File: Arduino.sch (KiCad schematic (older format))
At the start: 25 parts, among them J1 ISP, SW1 Reset, U1 ATMEGA32U4-AU, Y1 16MHz

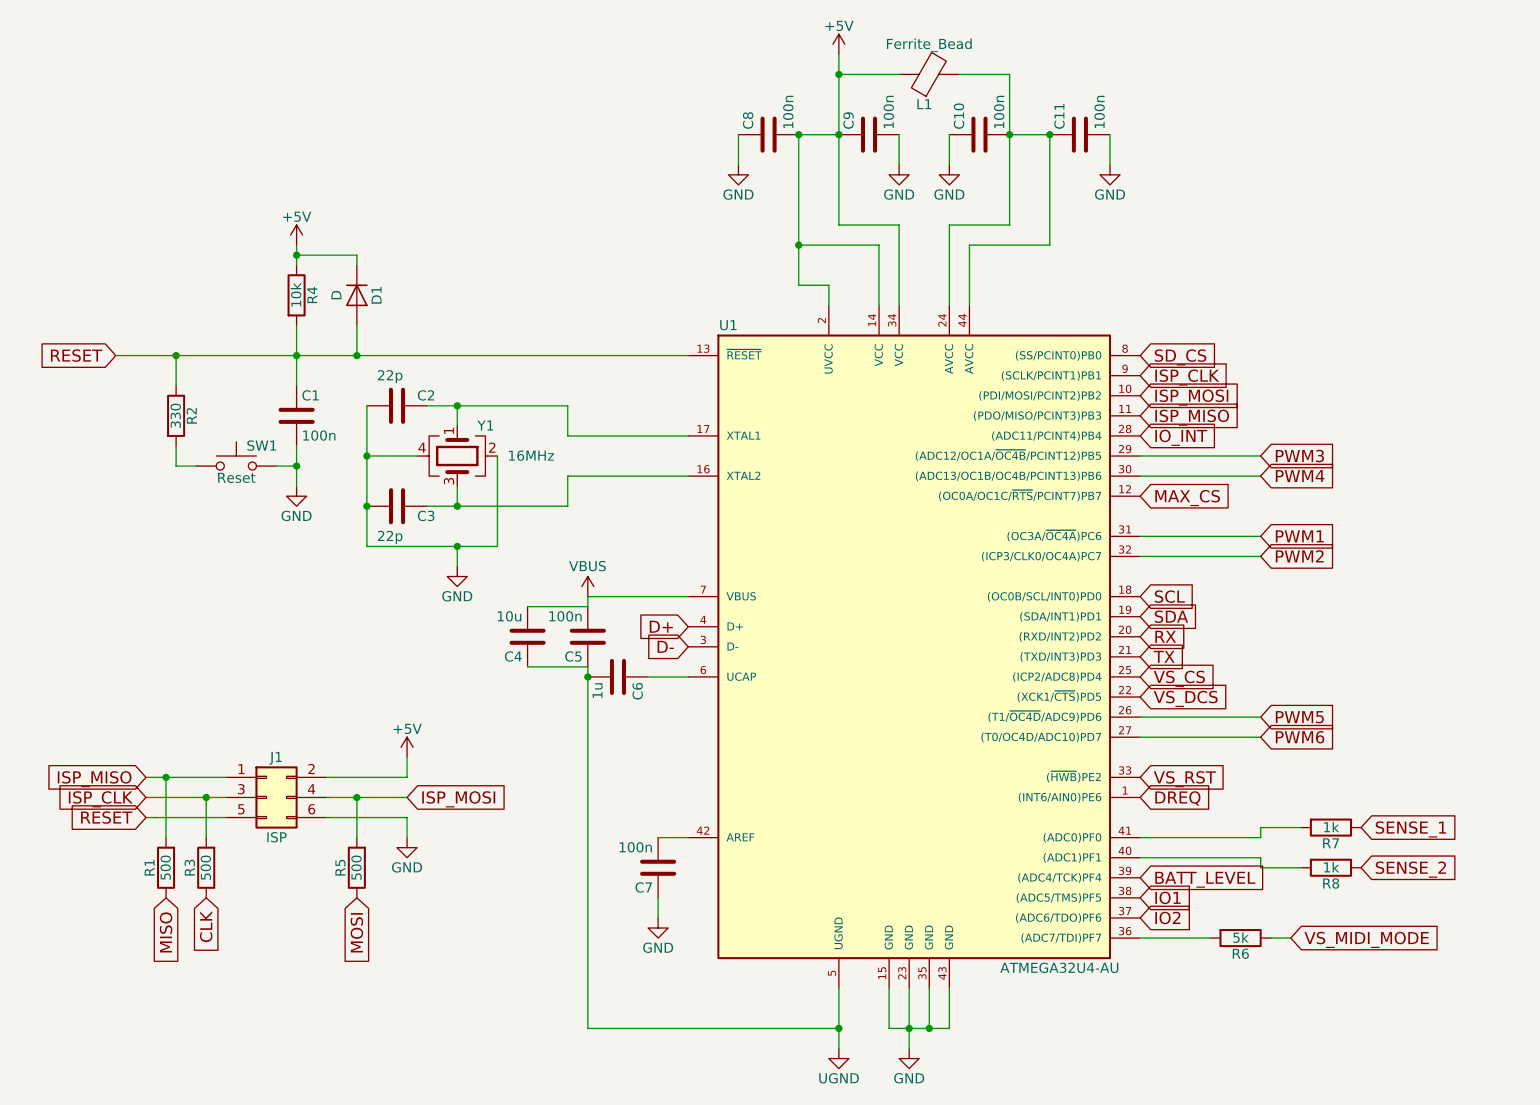
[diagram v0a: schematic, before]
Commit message: Board should be ok. Bargraph leds yet to do.
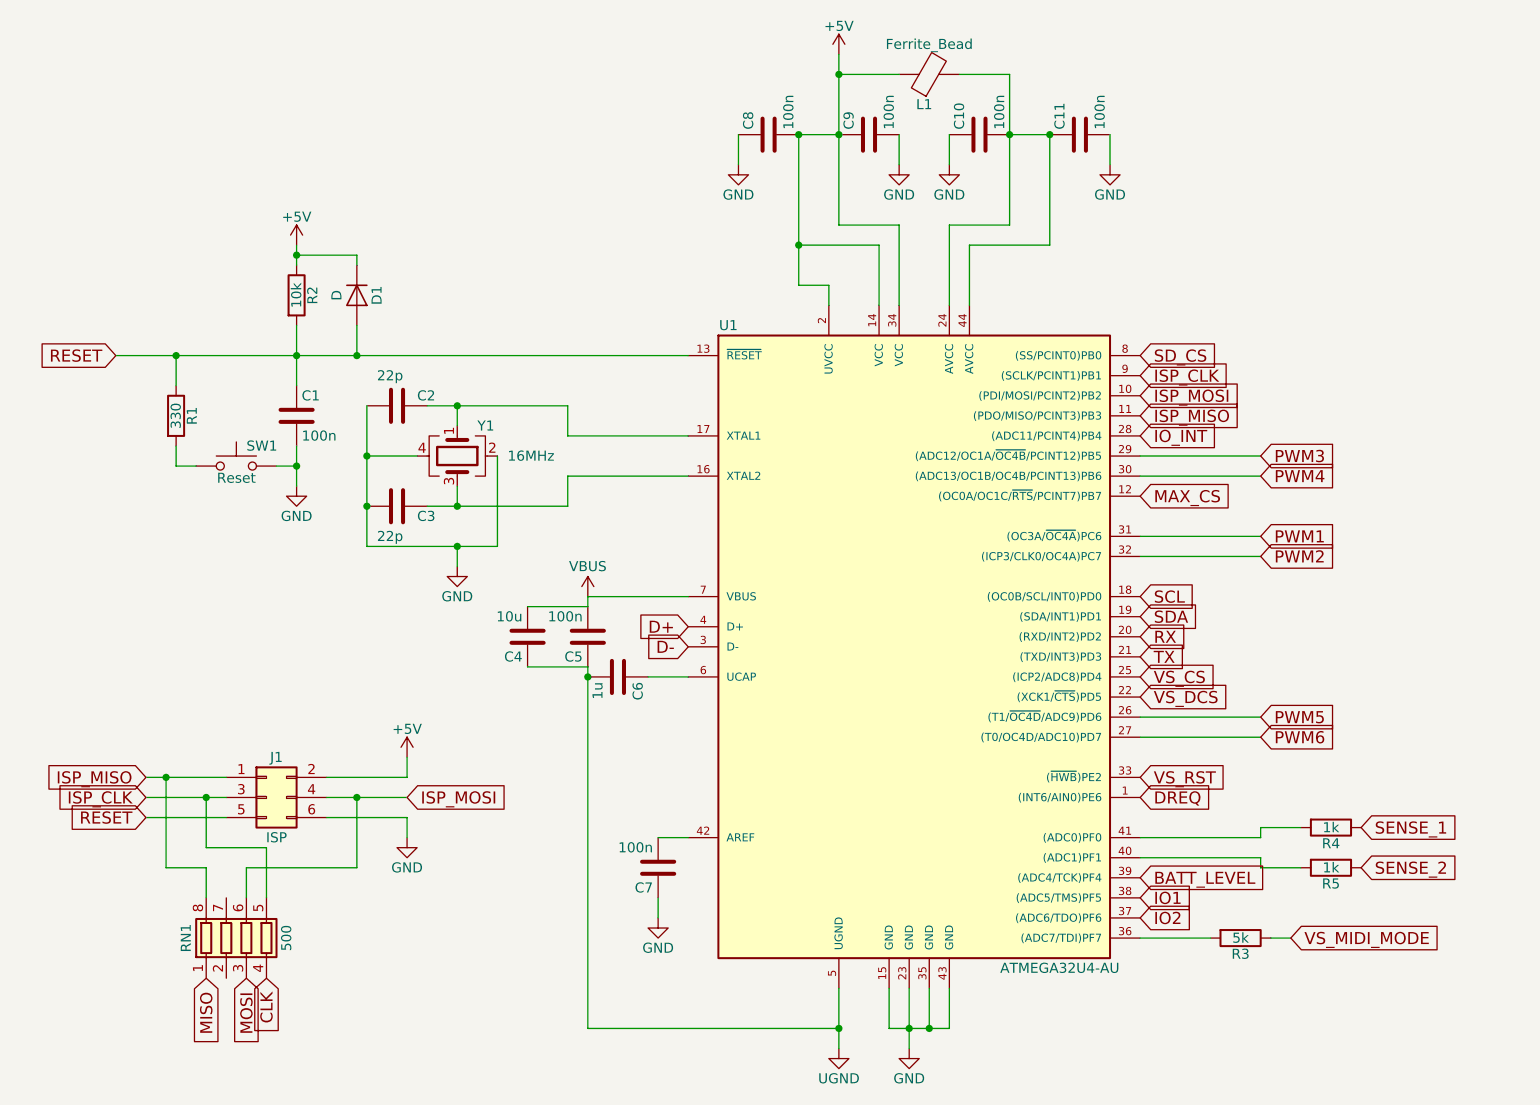
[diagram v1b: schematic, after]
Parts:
- removed R1, R3, R5: 500, Resistors_SMD:R_0603, symbol R
- added RN1: 500, Resistors_SMD:R_Array_Concave_4x0603, symbol R_Pack04
- renumbered R2 to R1, R4 to R2, R6 to R3, R7 to R4, R8 to R5
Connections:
- net CLK: now also RN1.4 (R4.1)
- net ISP_CLK: now also RN1.5 (R4.2)
- net ISP_MISO: now also RN1.8 (R1.2)
- net ISP_MOSI: now also RN1.6 (R3.2)
- net MISO: now also RN1.1 (R1.1)
- net MOSI: now also RN1.3 (R3.1)
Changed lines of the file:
@@
 RESET
 $Comp
-L R R4
+L R R2
 U 1 1 59A745F3
 P 1950 2050
-F 0 "R4" V 2030 2050 50  0000 C CNN
+F 0 "R2" V 2030 2050 50  0000 C CNN
 F 1 "10k" V 1950 2050 50  0000 C CNN
 F 2 "Resistors_SMD:R_0603" V 1880 2050 50  0001 C CNN
@@
 $EndComp
 $Comp
-L R R2
+L R R1
 U 1 1 59A75000
 P 1350 2650
-F 0 "R2" V 1430 2650 50  0000 C CNN
+F 0 "R1" V 1430 2650 50  0000 C CNN
 F 1 "330" V 1350 2650 50  0000 C CNN
 F 2 "Resistors_SMD:R_0603" V 1280 2650 50  0001 C CNN
@@
 	1    2500 4350
 	1    0    0    -1
-$EndComp
-$Comp
-L R R5
-U 1 1 59A7C3EE
-P 2250 4900
-F 0 "R5" V 2330 4900 50  0000 C CNN
-F 1 "500" V 2250 4900 50  0000 C CNN
-F 2 "Resistors_SMD:R_0603" V 2180 4900 50  0001 C CNN
-F 3 "" H 2250 4900 50  0001 C CNN
-	1    2250 4900
-	-1   0    0    1
 $EndComp
 Text GLabel 6150 2450 2    60   Input ~ 0
@@
 	1    0    0    -1
 $EndComp
-$Comp
-L R R1
-U 1 1 59A7CE6D
-P 1300 4900
-F 0 "R1" V 1380 4900 50  0000 C CNN
-F 1 "500" V 1300 4900 50  0000 C CNN
-F 2 "Resistors_SMD:R_0603" V 1230 4900 50  0001 C CNN
-F 3 "" H 1300 4900 50  0001 C CNN
-	1    1300 4900
-	-1   0    0    1
-$EndComp
-$Comp
-L R R3
-U 1 1 59A7CEDD
-P 1500 4900
-F 0 "R3" V 1580 4900 50  0000 C CNN
-F 1 "500" V 1500 4900 50  0000 C CNN
-F 2 "Resistors_SMD:R_0603" V 1430 4900 50  0001 C CNN
-F 3 "" H 1500 4900 50  0001 C CNN
-	1    1500 4900
-	-1   0    0    1
-$EndComp
-Text GLabel 1300 5050 3    60   Input ~ 0
+Text GLabel 1500 5450 3    60   Input ~ 0
 MISO
-Text GLabel 2250 5050 3    60   Input ~ 0
+Text GLabel 1700 5450 3    60   Input ~ 0
 MOSI
-Text GLabel 1500 5050 3    60   Input ~ 0
+Text GLabel 1800 5450 3    60   Input ~ 0
 CLK
 $Comp
@@
 	2500 4450 2500 4350
 Wire Wire Line
-	1300 4750 1300 4450
+	1300 4450 1300 4900
 Connection ~ 1300 4450
 Wire Wire Line
-	1500 4750 1500 4550
+	1500 4550 1500 4800
 Connection ~ 1500 4550
 Wire Wire Line
-	2250 4550 2250 4750
+	2250 4550 2250 4900
 Connection ~ 2250 4550
 Wire Wire Line
@@
 VS_MIDI_MODE
 $Comp
-L R R6
+L R R3
 U 1 1 59B1BBE0
 P 6650 5250
-F 0 "R6" V 6730 5250 50  0000 C CNN
+F 0 "R3" V 6730 5250 50  0000 C CNN
 F 1 "5k" V 6650 5250 50  0000 C CNN
 F 2 "Resistors_SMD:R_0603" V 6580 5250 50  0001 C CNN
@@
 	6800 5250 6900 5250
 $Comp
-L R R7
+L R R4
 U 1 1 59C9C3BA
 P 7100 4700
-F 0 "R7" V 7180 4700 50  0000 C CNN
+F 0 "R4" V 7180 4700 50  0000 C CNN
 F 1 "1k" V 7100 4700 50  0000 C CNN
 F 2 "Resistors_SMD:R_0603" V 7030 4700 50  0001 C CNN
@@
 $EndComp
 $Comp
-L R R8
+L R R5
 U 1 1 59C9C547
 P 7100 4900
-F 0 "R8" V 7180 4900 50  0000 C CNN
+F 0 "R5" V 7180 4900 50  0000 C CNN
 F 1 "1k" V 7100 4900 50  0000 C CNN
 F 2 "Resistors_SMD:R_0603" V 7030 4900 50  0001 C CNN
@@
 Wire Wire Line
 	6750 4850 6150 4850
+$Comp
+L R_Pack04 RN1
+U 1 1 59CC0F73
+P 1700 5250
+F 0 "RN1" V 1400 5250 50  0000 C CNN
+F 1 "500" V 1900 5250 50  0000 C CNN
+F 2 "Resistors_SMD:R_Array_Concave_4x0603" V 1975 5250 50  0001 C CNN
+F 3 "" H 1700 5250 50  0001 C CNN
+	1    1700 5250
+	1    0    0    -1
+$EndComp
+Wire Wire Line
+	1300 4900 1500 4900
+Wire Wire Line
+	1500 4900 1500 5050
+Wire Wire Line
+	2250 4900 1700 4900
+Wire Wire Line
+	1700 4900 1700 5050
+Wire Wire Line
+	1500 4800 1800 4800
+Wire Wire Line
+	1800 4800 1800 5050
 $EndSCHEMATC

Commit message: Board modified after ckecking. Ready for fab, just need to create gerber, position and components files.
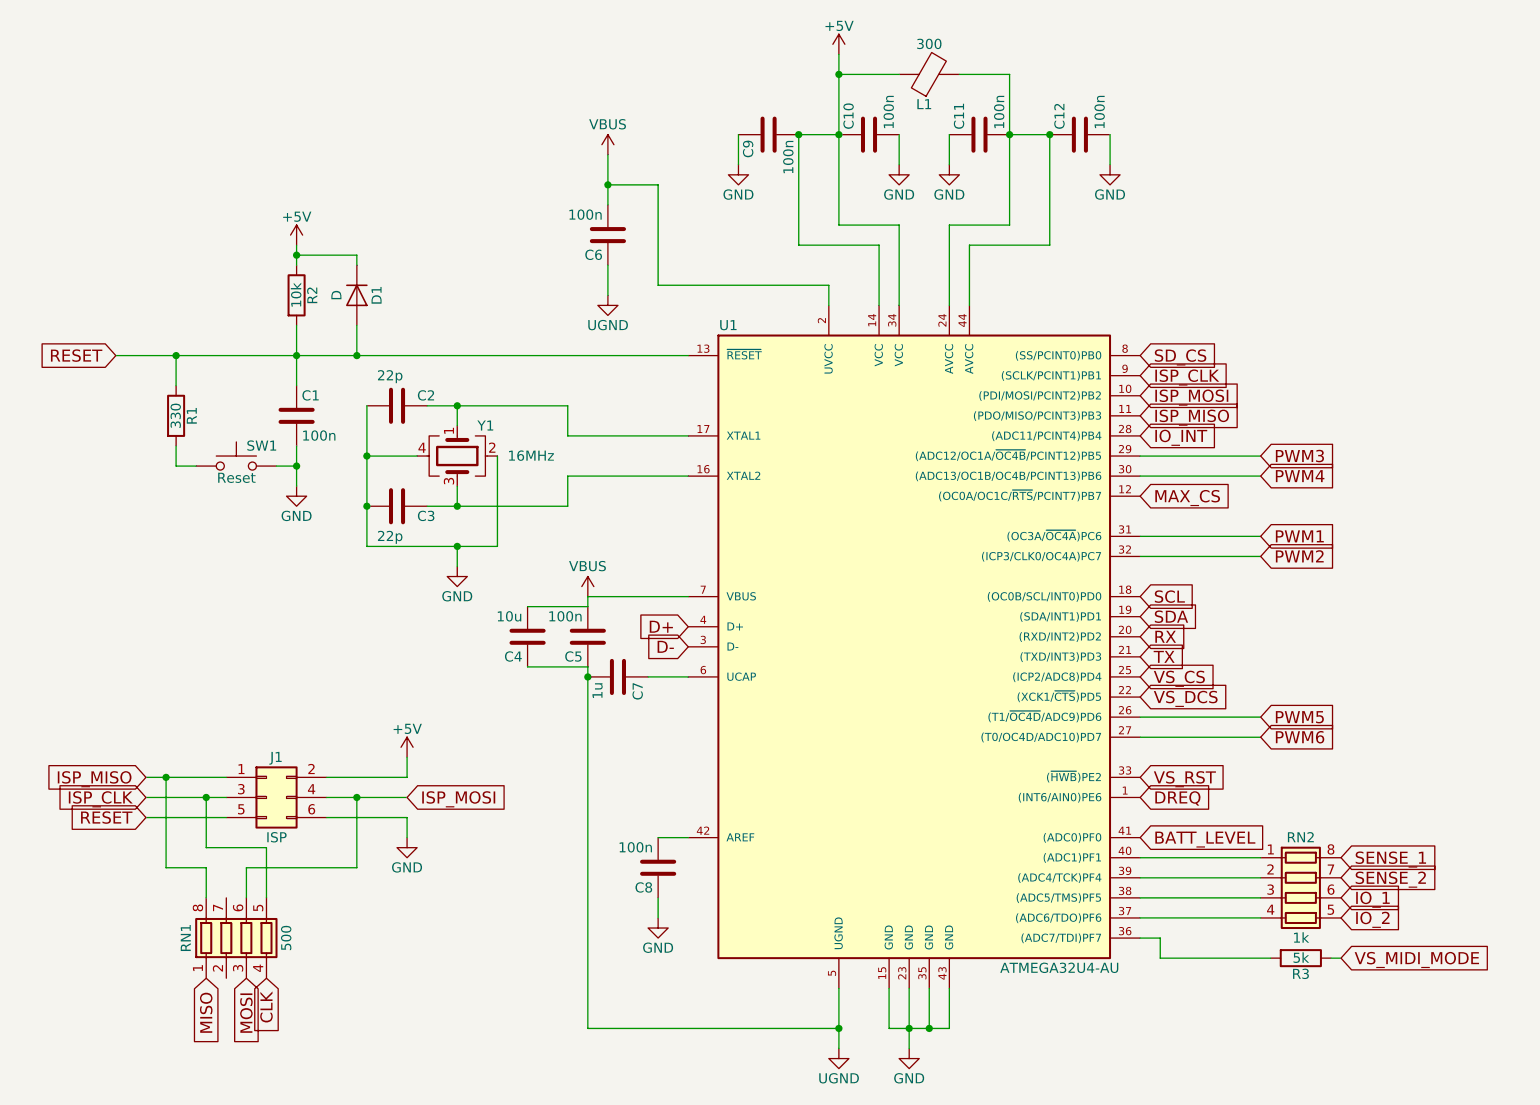
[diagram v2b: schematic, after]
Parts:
- removed R4, R5: 1k, Resistors_SMD:R_0603, symbol R
- added C6: 100n, Capacitors_SMD:C_0603, symbol C
- added RN2: 1k, Resistors_SMD:R_Array_Concave_4x0603, symbol R_Pack04
- L1: value Ferrite_Bead -> 300
- renumbered C9 to C10, C10 to C11, C11 to C12, C6 to C7, C7 to C8, C8 to C9
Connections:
- net +5V: no longer U1.2 (UVCC)
- net BATT_LEVEL: now also U1.41 ((ADC0)PF0); no longer U1.39 ((ADC4/TCK)PF4)
- net SENSE_1: now also RN2.8 (R1.2)
- net SENSE_2: now also RN2.7 (R2.2)
- net UGND: now also C6.1
- net VBUS: now also U1.2 (UVCC), C6.2
- net at U1.40 ((ADC1)PF1): now also RN2.1 (R1.1)
- net IO1: no longer names the net of U1.38 ((ADC5/TMS)PF5)
- net IO1: now also RN2.3 (R3.1)
- net IO2: no longer names the net of U1.37 ((ADC6/TDO)PF6)
- net IO2: now also RN2.4 (R4.1)
- new net: RN2.2 (R2.1), U1.39 ((ADC4/TCK)PF4)
- new net IO_1: RN2.6 (R3.2)
- new net IO_2: RN2.5 (R4.2)
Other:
- moved on the sheet: R3
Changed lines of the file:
@@
 EESchema Schematic File Version 2
+LIBS:ContactConsequencesMono-rescue
 LIBS:switches-perso
 LIBS:Logos
@@
 $EndComp
 $Comp
-L C C9
+L C C10
 U 1 1 59A733E9
 P 4800 1250
-F 0 "C9" H 4825 1350 50  0000 L CNN
+F 0 "C10" H 4825 1350 50  0000 L CNN
 F 1 "100n" H 4825 1150 50  0000 L CNN
 F 2 "Capacitors_SMD:C_0603" H 4838 1100 50  0001 C CNN
@@
 $EndComp
 $Comp
-L C C8
+L C C9
 U 1 1 59A734B6
 P 4300 1250
-F 0 "C8" H 4325 1350 50  0000 L CNN
+F 0 "C9" H 4325 1350 50  0000 L CNN
 F 1 "100n" H 4325 1150 50  0000 L CNN
 F 2 "Capacitors_SMD:C_0603" H 4338 1100 50  0001 C CNN
 F 3 "" H 4300 1250 50  0001 C CNN
 	1    4300 1250
-	0    -1   -1   0
+	0    -1   1    0
 $EndComp
 $Comp
@@
 $EndComp
 $Comp
-L C C10
+L C C11
 U 1 1 59A74301
 P 5350 1250
-F 0 "C10" H 5375 1350 50  0000 L CNN
+F 0 "C11" H 5375 1350 50  0000 L CNN
 F 1 "100n" H 5375 1150 50  0000 L CNN
 F 2 "Capacitors_SMD:C_0603" H 5388 1100 50  0001 C CNN
@@
 $EndComp
 $Comp
-L C C11
+L C C12
 U 1 1 59A7433B
 P 5850 1250
-F 0 "C11" H 5875 1350 50  0000 L CNN
+F 0 "C12" H 5875 1350 50  0000 L CNN
 F 1 "100n" H 5875 1150 50  0000 L CNN
 F 2 "Capacitors_SMD:C_0603" H 5888 1100 50  0001 C CNN
@@
 $EndComp
 $Comp
-L C C6
+L C C7
 U 1 1 59A9524E
 P 3550 3950
-F 0 "C6" H 3575 4050 50  0000 L CNN
+F 0 "C7" H 3575 4050 50  0000 L CNN
 F 1 "1u" H 3575 3850 50  0000 L CNN
 F 2 "Capacitors_SMD:C_0603" H 3588 3800 50  0001 C CNN
@@
 D+
 $Comp
-L C C7
+L C C8
 U 1 1 59A9601B
 P 3750 4900
-F 0 "C7" H 3775 5000 50  0000 L CNN
+F 0 "C8" H 3775 5000 50  0000 L CNN
 F 1 "100n" H 3775 4800 50  0000 L CNN
 F 2 "Capacitors_SMD:C_0603" H 3788 4750 50  0001 C CNN
@@
 Text GLabel 6150 3850 2    60   Input ~ 0
 TX
-Text GLabel 7250 4700 2    60   Input ~ 0
+Text GLabel 7150 4850 2    60   Input ~ 0
 SENSE_1
-Text GLabel 7250 4900 2    60   Input ~ 0
+Text GLabel 7150 4950 2    60   Input ~ 0
 SENSE_2
 Text GLabel 6150 2350 2    60   Input ~ 0
@@
 P 5100 950
 F 0 "L1" V 4950 975 50  0000 C CNN
-F 1 "Ferrite_Bead" V 5250 950 50  0000 C CNN
+F 1 "300" V 5250 950 50  0000 C CNN
 F 2 "Inductors_SMD:L_0603" V 5030 950 50  0001 C CNN
 F 3 "" H 5100 950 50  0001 C CNN
@@
 	0    -1   -1   0
 $EndComp
-Text GLabel 6150 4950 2    60   Input ~ 0
+Text GLabel 6150 4750 2    60   Input ~ 0
 BATT_LEVEL
 Text GLabel 6150 4450 2    60   Input ~ 0
@@
 Wire Wire Line
 	6150 4250 6750 4250
-Text GLabel 6150 5050 2    60   Input ~ 0
-IO1
-Text GLabel 6150 5150 2    60   Input ~ 0
-IO2
+Text GLabel 7150 5050 2    60   Input ~ 0
+IO_1
+Text GLabel 7150 5150 2    60   Input ~ 0
+IO_2
 Wire Wire Line
 	4450 1250 4650 1250
 Wire Wire Line
 	4850 1800 4450 1800
-Wire Wire Line
-	4450 1250 4450 2000
 Connection ~ 4450 1250
 Wire Wire Line
 	4600 2100 4600 2000
-Wire Wire Line
-	4600 2000 4450 2000
-Connection ~ 4450 1800
 Wire Wire Line
 	5300 1800 5300 2100
 Text GLabel 6150 2750 2    60   Input ~ 0
 IO_INT
-Text GLabel 6900 5250 2    60   Input ~ 0
+Text GLabel 7150 5350 2    60   Input ~ 0
 VS_MIDI_MODE
 $Comp
 L R R3
 U 1 1 59B1BBE0
-P 6650 5250
-F 0 "R3" V 6730 5250 50  0000 C CNN
-F 1 "5k" V 6650 5250 50  0000 C CNN
-F 2 "Resistors_SMD:R_0603" V 6580 5250 50  0001 C CNN
-F 3 "" H 6650 5250 50  0001 C CNN
-	1    6650 5250
+P 6950 5350
+F 0 "R3" V 7030 5350 50  0000 C CNN
+F 1 "5k" V 6950 5350 50  0000 C CNN
+F 2 "Resistors_SMD:R_0603" V 6880 5350 50  0001 C CNN
+F 3 "" H 6950 5350 50  0001 C CNN
+	1    6950 5350
 	0    1    1    0
 $EndComp
-Wire Wire Line
-	6150 5250 6500 5250
-Wire Wire Line
-	6800 5250 6900 5250
-$Comp
-L R R4
-U 1 1 59C9C3BA
-P 7100 4700
-F 0 "R4" V 7180 4700 50  0000 C CNN
-F 1 "1k" V 7100 4700 50  0000 C CNN
-F 2 "Resistors_SMD:R_0603" V 7030 4700 50  0001 C CNN
-F 3 "" H 7100 4700 50  0001 C CNN
-	1    7100 4700
-	0    1    1    0
-$EndComp
-$Comp
-L R R5
-U 1 1 59C9C547
-P 7100 4900
-F 0 "R5" V 7180 4900 50  0000 C CNN
-F 1 "1k" V 7100 4900 50  0000 C CNN
-F 2 "Resistors_SMD:R_0603" V 7030 4900 50  0001 C CNN
-F 3 "" H 7100 4900 50  0001 C CNN
-	1    7100 4900
-	0    1    1    0
-$EndComp
-Wire Wire Line
-	6150 4750 6750 4750
-Wire Wire Line
-	6750 4750 6750 4700
-Wire Wire Line
-	6750 4700 6950 4700
-Wire Wire Line
-	6950 4900 6750 4900
-Wire Wire Line
-	6750 4900 6750 4850
-Wire Wire Line
-	6750 4850 6150 4850
 $Comp
 L R_Pack04 RN1
@@
 Wire Wire Line
 	1800 4800 1800 5050
+Wire Wire Line
+	4450 1800 4450 1250
+$Comp
+L VBUS #PWR015
+U 1 1 59F06B7F
+P 3500 1350
+F 0 "#PWR015" H 3500 1200 50  0001 C CNN
+F 1 "VBUS" H 3500 1500 50  0000 C CNN
+F 2 "" H 3500 1350 50  0001 C CNN
+F 3 "" H 3500 1350 50  0001 C CNN
+	1    3500 1350
+	1    0    0    -1
+$EndComp
+$Comp
+L C C6
+U 1 1 59F06C60
+P 3500 1750
+F 0 "C6" H 3525 1850 50  0000 L CNN
+F 1 "100n" H 3525 1650 50  0000 L CNN
+F 2 "Capacitors_SMD:C_0603" H 3538 1600 50  0001 C CNN
+F 3 "" H 3500 1750 50  0001 C CNN
+	1    3500 1750
+	-1   0    0    1
+$EndComp
+Wire Wire Line
+	3500 1350 3500 1600
+Wire Wire Line
+	3500 1500 3750 1500
+Wire Wire Line
+	3750 1500 3750 2000
+Wire Wire Line
+	3750 2000 4600 2000
+Connection ~ 3500 1500
+$Comp
+L UGND #PWR016
+U 1 1 59F07092
+P 3500 2050
+F 0 "#PWR016" H 3500 1800 50  0001 C CNN
+F 1 "UGND" H 3500 1900 50  0000 C CNN
+F 2 "" H 3500 2050 50  0001 C CNN
+F 3 "" H 3500 2050 50  0001 C CNN
+	1    3500 2050
+	1    0    0    -1
+$EndComp
+Wire Wire Line
+	3500 1900 3500 2050
+$Comp
+L R_Pack04 RN2
+U 1 1 59F9C5BE
+P 6950 5050
+F 0 "RN2" V 6650 5050 50  0000 C CNN
+F 1 "1k" V 7150 5050 50  0000 C CNN
+F 2 "Resistors_SMD:R_Array_Concave_4x0603" V 7225 5050 50  0001 C CNN
+F 3 "" H 6950 5050 50  0001 C CNN
+	1    6950 5050
+	0    1    1    0
+$EndComp
+Wire Wire Line
+	6150 5250 6250 5250
+Wire Wire Line
+	6150 4850 6750 4850
+Wire Wire Line
+	6150 4950 6750 4950
+Wire Wire Line
+	6150 5050 6750 5050
+Wire Wire Line
+	6150 5150 6750 5150
+Wire Wire Line
+	6250 5250 6250 5350
+Wire Wire Line
+	6250 5350 6800 5350
+Wire Wire Line
+	7100 5350 7150 5350
 $EndSCHEMATC
